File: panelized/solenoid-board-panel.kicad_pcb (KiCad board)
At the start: 2 copper layers, 99 x 94.5 mm, 216 parts, among them J1 JST_PH, J2 0.1" header, Q1 FDN339AN

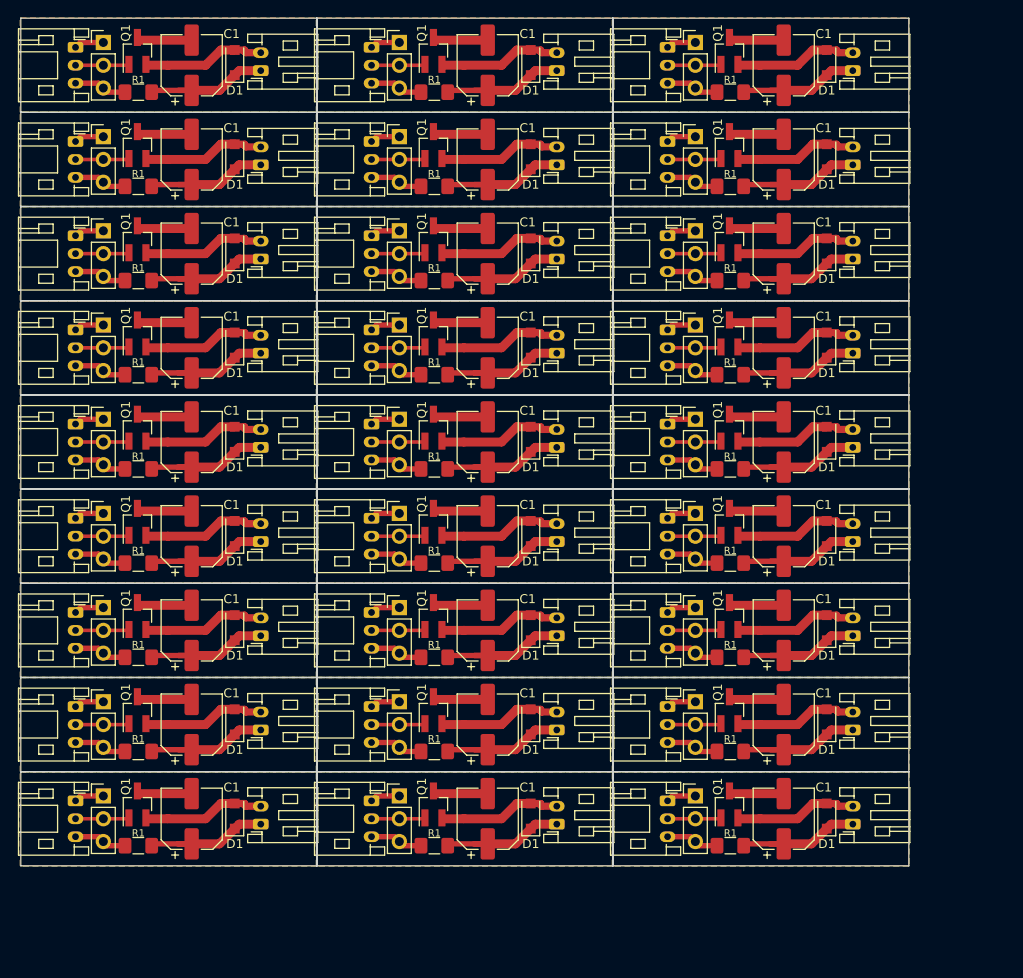
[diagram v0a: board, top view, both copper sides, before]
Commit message: updated panelized design
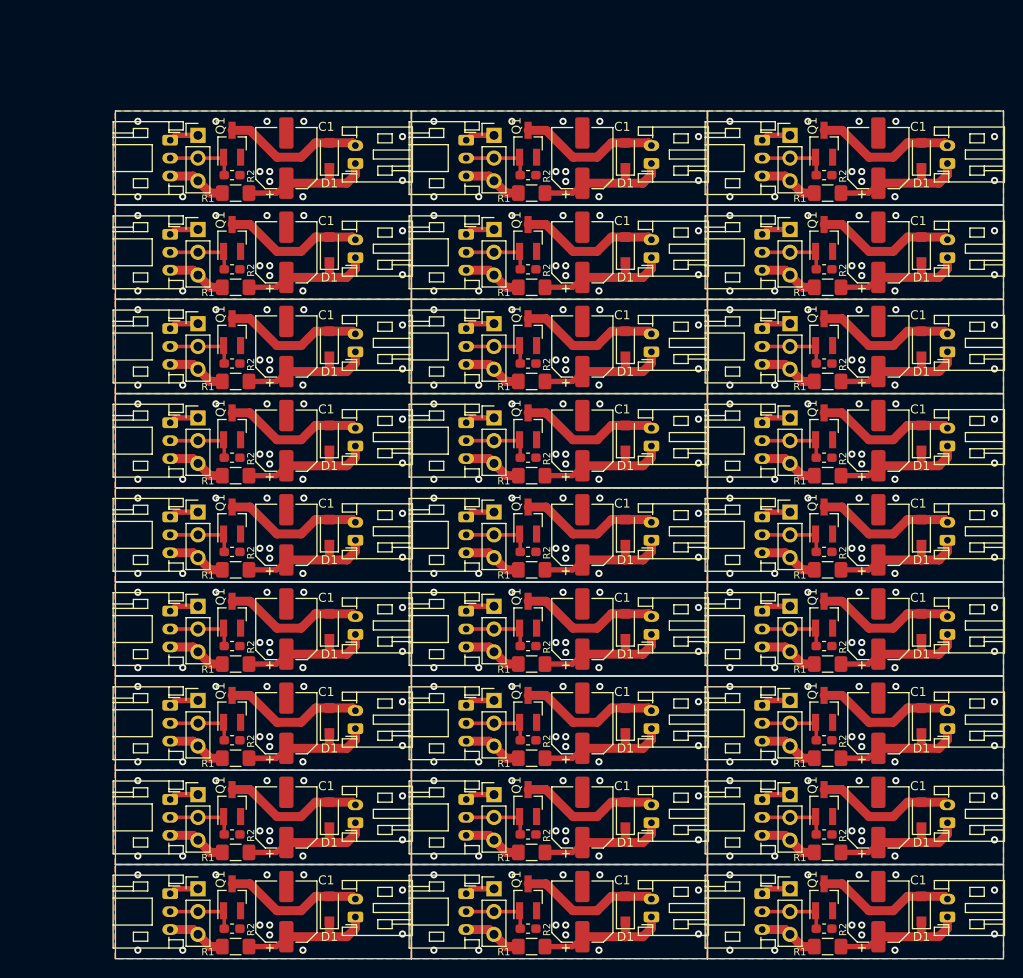
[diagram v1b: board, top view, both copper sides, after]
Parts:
- removed the C1 at (95.0, 99.2)
- removed the C1 at (95.0, 67.8)
- removed the C1 at (62.0, 67.8)
- removed the C1 at (29.1, 67.8)
- removed the C1 at (95.0, 57.2)
- removed the C1 at (62.0, 57.2)
- removed the C1 at (29.1, 57.2)
- removed the C1 at (95.0, 46.8)
- removed the C1 at (62.0, 46.8)
- removed the C1 at (29.1, 46.8)
- removed the C1 at (95.0, 36.2)
- removed the C1 at (62.0, 99.2)
- removed the C1 at (62.0, 36.2)
- removed the C1 at (29.1, 36.2)
- removed the C1 at (95.0, 25.8)
- removed the C1 at (62.0, 25.8)
- removed the C1 at (29.1, 25.8)
- removed the C1 at (95.0, 15.2)
- removed the C1 at (62.0, 15.2)
- removed the C1 at (29.1, 99.2)
- removed the C1 at (95.0, 88.8)
- removed the C1 at (62.0, 88.8)
- removed the C1 at (29.1, 88.8)
- removed the C1 at (95.0, 78.2)
- removed the C1 at (62.0, 78.2)
- removed the C1 at (29.1, 78.2)
- removed the D1 at (99.8, 99.0)
- removed the D1 at (99.8, 67.5)
- removed the D1 at (66.8, 67.5)
- removed the D1 at (33.9, 67.5)
- removed the D1 at (99.8, 57.0)
- removed the D1 at (66.8, 57.0)
- removed the D1 at (33.9, 57.0)
- removed the D1 at (99.8, 46.5)
- removed the D1 at (66.8, 46.5)
- removed the D1 at (33.9, 46.5)
- removed the D1 at (99.8, 36.0)
- removed the D1 at (66.8, 99.0)
- removed the D1 at (66.8, 36.0)
- removed the D1 at (33.9, 36.0)
- removed the D1 at (99.8, 25.4)
- removed the D1 at (66.8, 25.4)
- removed the D1 at (33.9, 25.4)
- removed the D1 at (99.8, 14.9)
- removed the D1 at (66.8, 14.9)
- removed the D1 at (33.9, 99.0)
- removed the D1 at (99.8, 88.5)
- removed the D1 at (66.8, 88.5)
- removed the D1 at (33.9, 88.5)
- removed the D1 at (99.8, 78.0)
- removed the D1 at (66.8, 78.0)
- removed the D1 at (33.9, 78.0)
- removed the G*** at (93.8, 99.8)
- removed the G*** at (93.8, 68.2)
- removed the G*** at (60.8, 68.2)
- removed the G*** at (27.8, 68.2)
- removed the G*** at (93.8, 57.8)
- removed the G*** at (60.8, 57.8)
- removed the G*** at (27.8, 57.8)
- removed the G*** at (93.8, 47.2)
- removed the G*** at (60.8, 47.2)
- removed the G*** at (27.8, 47.2)
- removed the G*** at (93.8, 36.8)
- removed the G*** at (60.8, 99.8)
- removed the G*** at (60.8, 36.8)
- removed the G*** at (27.8, 36.8)
- removed the G*** at (93.8, 26.2)
- removed the G*** at (60.8, 26.2)
- removed the G*** at (27.8, 26.2)
- removed the G*** at (93.8, 15.8)
- removed the G*** at (60.8, 15.8)
- removed the G*** at (27.8, 99.8)
- removed the G*** at (93.8, 89.2)
- removed the G*** at (60.8, 89.2)
- removed the G*** at (27.8, 89.2)
- removed the G*** at (93.8, 78.8)
- removed the G*** at (60.8, 78.8)
- removed the G*** at (27.8, 78.8)
- removed the J1 at (82.1, 97.2)
- removed the J1 at (82.1, 65.8)
- removed the J1 at (49.1, 65.8)
- removed the J1 at (16.1, 65.8)
- removed the J1 at (82.1, 55.2)
- removed the J1 at (49.1, 55.2)
- removed the J1 at (16.1, 55.2)
- removed the J1 at (82.1, 44.8)
- removed the J1 at (49.1, 44.8)
- removed the J1 at (16.1, 44.8)
- removed the J1 at (82.1, 34.2)
- removed the J1 at (49.1, 97.2)
- removed the J1 at (49.1, 34.2)
- removed the J1 at (16.1, 34.2)
- removed the J1 at (82.1, 23.8)
- removed the J1 at (49.1, 23.8)
- removed the J1 at (16.1, 23.8)
- removed the J1 at (82.1, 13.2)
- removed the J1 at (49.1, 13.2)
- removed the J1 at (16.1, 97.2)
- removed the J1 at (82.1, 86.8)
- removed the J1 at (49.1, 86.8)
- removed the J1 at (16.1, 86.8)
- removed the J1 at (82.1, 76.2)
- removed the J1 at (49.1, 76.2)
- removed the J1 at (16.1, 76.2)
- removed the J2 at (85.2, 96.7)
- removed the J2 at (85.2, 65.2)
- removed the J2 at (52.2, 65.2)
- removed the J2 at (19.2, 65.2)
- removed the J2 at (85.2, 54.7)
- removed the J2 at (52.2, 54.7)
- removed the J2 at (19.2, 54.7)
- removed the J2 at (85.2, 44.2)
- removed the J2 at (52.2, 44.2)
- removed the J2 at (19.2, 44.2)
- removed the J2 at (85.2, 33.7)
- removed the J2 at (52.2, 96.7)
- removed the J2 at (52.2, 33.7)
- removed the J2 at (19.2, 33.7)
- removed the J2 at (85.2, 23.2)
- removed the J2 at (52.2, 23.2)
- removed the J2 at (19.2, 23.2)
- removed the J2 at (85.2, 12.7)
- removed the J2 at (52.2, 12.7)
- removed the J2 at (19.2, 96.7)
- removed the J2 at (85.2, 86.2)
- removed the J2 at (52.2, 86.2)
- removed the J2 at (19.2, 86.2)
- removed the J2 at (85.2, 75.7)
- removed the J2 at (52.2, 75.7)
- removed the J2 at (19.2, 75.7)
- removed the L1 at (102.8, 99.8)
- removed the L1 at (102.8, 68.3)
- removed the L1 at (69.8, 68.3)
- removed the L1 at (36.8, 68.3)
- removed the L1 at (102.8, 57.9)
- removed the L1 at (69.8, 57.9)
- removed the L1 at (36.8, 57.9)
- removed the L1 at (102.8, 47.4)
- removed the L1 at (69.8, 47.4)
- removed the L1 at (36.8, 47.4)
- removed the L1 at (102.8, 36.9)
- removed the L1 at (69.8, 99.8)
- removed the L1 at (69.8, 36.9)
- removed the L1 at (36.8, 36.9)
- removed the L1 at (102.8, 26.4)
- removed the L1 at (69.8, 26.4)
- removed the L1 at (36.8, 26.4)
- removed the L1 at (102.8, 15.8)
- removed the L1 at (69.8, 15.8)
- removed the L1 at (36.8, 99.8)
- removed the L1 at (102.8, 89.3)
- removed the L1 at (69.8, 89.3)
- removed the L1 at (36.8, 89.3)
- removed the L1 at (102.8, 78.8)
- removed the L1 at (69.8, 78.8)
- removed the L1 at (36.8, 78.8)
- removed the Q1 at (89.0, 97.7)
- removed the Q1 at (89.0, 66.2)
- removed the Q1 at (56.0, 66.2)
- removed the Q1 at (23.0, 66.2)
- removed the Q1 at (89.0, 55.6)
- removed the Q1 at (56.0, 55.6)
- removed the Q1 at (23.0, 55.6)
- removed the Q1 at (89.0, 45.1)
- removed the Q1 at (56.0, 45.1)
- removed the Q1 at (23.0, 45.1)
- removed the Q1 at (89.0, 34.6)
- removed the Q1 at (56.0, 97.7)
- removed the Q1 at (56.0, 34.6)
- removed the Q1 at (23.0, 34.6)
- removed the Q1 at (89.0, 24.1)
- removed the Q1 at (56.0, 24.1)
- removed the Q1 at (23.0, 24.1)
- removed the Q1 at (89.0, 13.7)
- removed the Q1 at (56.0, 13.7)
- removed the Q1 at (23.0, 97.7)
- removed the Q1 at (89.0, 87.2)
- removed the Q1 at (56.0, 87.2)
- removed the Q1 at (23.0, 87.2)
- removed the Q1 at (89.0, 76.7)
- removed the Q1 at (56.0, 76.7)
- removed the Q1 at (23.0, 76.7)
- removed the R1 at (89.1, 102.2)
- removed the R1 at (89.1, 70.8)
- removed the R1 at (56.1, 70.8)
- removed the R1 at (23.1, 70.8)
- removed the R1 at (89.1, 60.2)
- removed the R1 at (56.1, 60.2)
- removed the R1 at (23.1, 60.2)
- removed the R1 at (89.1, 49.8)
- removed the R1 at (56.1, 49.8)
- removed the R1 at (23.1, 49.8)
- removed the R1 at (89.1, 39.2)
- removed the R1 at (56.1, 102.2)
- removed the R1 at (56.1, 39.2)
- removed the R1 at (23.1, 39.2)
- removed the R1 at (89.1, 28.8)
- removed the R1 at (56.1, 28.8)
- removed the R1 at (23.1, 28.8)
- removed the R1 at (89.1, 18.2)
- removed the R1 at (56.1, 18.2)
- removed the R1 at (23.1, 102.2)
- removed the R1 at (89.1, 91.8)
- removed the R1 at (56.1, 91.8)
- removed the R1 at (23.1, 91.8)
- removed the R1 at (89.1, 81.2)
- removed the R1 at (56.1, 81.2)
- removed the R1 at (23.1, 81.2)
- added C1: 220uF, Capacitor_SMD:CP_Elec_6.3x5.4, F.Cu at (105.6, 109.6)
- added C1: 220uF, Capacitor_SMD:CP_Elec_6.3x5.4, F.Cu at (105.6, 78.1)
- added C1: 220uF, Capacitor_SMD:CP_Elec_6.3x5.4, F.Cu at (72.6, 78.1)
- added C1: 220uF, Capacitor_SMD:CP_Elec_6.3x5.4, F.Cu at (39.6, 78.1)
- added C1: 220uF, Capacitor_SMD:CP_Elec_6.3x5.4, F.Cu at (105.6, 67.6)
- added C1: 220uF, Capacitor_SMD:CP_Elec_6.3x5.4, F.Cu at (72.6, 67.6)
- added C1: 220uF, Capacitor_SMD:CP_Elec_6.3x5.4, F.Cu at (39.6, 67.6)
- added C1: 220uF, Capacitor_SMD:CP_Elec_6.3x5.4, F.Cu at (105.6, 57.1)
- added C1: 220uF, Capacitor_SMD:CP_Elec_6.3x5.4, F.Cu at (72.6, 57.1)
- added C1: 220uF, Capacitor_SMD:CP_Elec_6.3x5.4, F.Cu at (39.6, 57.1)
- added C1: 220uF, Capacitor_SMD:CP_Elec_6.3x5.4, F.Cu at (105.6, 46.6)
- added C1: 220uF, Capacitor_SMD:CP_Elec_6.3x5.4, F.Cu at (72.6, 109.6)
- added C1: 220uF, Capacitor_SMD:CP_Elec_6.3x5.4, F.Cu at (72.6, 46.6)
- added C1: 220uF, Capacitor_SMD:CP_Elec_6.3x5.4, F.Cu at (39.6, 46.6)
- added C1: 220uF, Capacitor_SMD:CP_Elec_6.3x5.4, F.Cu at (105.6, 36.1)
- added C1: 220uF, Capacitor_SMD:CP_Elec_6.3x5.4, F.Cu at (72.6, 36.1)
- added C1: 220uF, Capacitor_SMD:CP_Elec_6.3x5.4, F.Cu at (39.6, 36.1)
- added C1: 220uF, Capacitor_SMD:CP_Elec_6.3x5.4, F.Cu at (105.6, 25.6)
- added C1: 220uF, Capacitor_SMD:CP_Elec_6.3x5.4, F.Cu at (72.6, 25.6)
- added C1: 220uF, Capacitor_SMD:CP_Elec_6.3x5.4, F.Cu at (39.6, 109.6)
- added C1: 220uF, Capacitor_SMD:CP_Elec_6.3x5.4, F.Cu at (105.6, 99.1)
- added C1: 220uF, Capacitor_SMD:CP_Elec_6.3x5.4, F.Cu at (72.6, 99.1)
- added C1: 220uF, Capacitor_SMD:CP_Elec_6.3x5.4, F.Cu at (39.6, 99.1)
- added C1: 220uF, Capacitor_SMD:CP_Elec_6.3x5.4, F.Cu at (105.6, 88.6)
- added C1: 220uF, Capacitor_SMD:CP_Elec_6.3x5.4, F.Cu at (72.6, 88.6)
- added C1: 220uF, Capacitor_SMD:CP_Elec_6.3x5.4, F.Cu at (39.6, 88.6)
- added D1: 1N4007L, Diode_SMD:D_SOD-123F, F.Cu at (110.4, 109.3)
- added D1: 1N4007L, Diode_SMD:D_SOD-123F, F.Cu at (110.4, 77.8)
- added D1: 1N4007L, Diode_SMD:D_SOD-123F, F.Cu at (77.4, 77.8)
- added D1: 1N4007L, Diode_SMD:D_SOD-123F, F.Cu at (44.4, 77.8)
- added D1: 1N4007L, Diode_SMD:D_SOD-123F, F.Cu at (110.4, 67.3)
- added D1: 1N4007L, Diode_SMD:D_SOD-123F, F.Cu at (77.4, 67.3)
- added D1: 1N4007L, Diode_SMD:D_SOD-123F, F.Cu at (44.4, 67.3)
- added D1: 1N4007L, Diode_SMD:D_SOD-123F, F.Cu at (110.4, 56.8)
- added D1: 1N4007L, Diode_SMD:D_SOD-123F, F.Cu at (77.4, 56.8)
- added D1: 1N4007L, Diode_SMD:D_SOD-123F, F.Cu at (44.4, 56.8)
- added D1: 1N4007L, Diode_SMD:D_SOD-123F, F.Cu at (110.4, 46.3)
- added D1: 1N4007L, Diode_SMD:D_SOD-123F, F.Cu at (77.4, 109.3)
- added D1: 1N4007L, Diode_SMD:D_SOD-123F, F.Cu at (77.4, 46.3)
- added D1: 1N4007L, Diode_SMD:D_SOD-123F, F.Cu at (44.4, 46.3)
- added D1: 1N4007L, Diode_SMD:D_SOD-123F, F.Cu at (110.4, 35.8)
- added D1: 1N4007L, Diode_SMD:D_SOD-123F, F.Cu at (77.4, 35.8)
- added D1: 1N4007L, Diode_SMD:D_SOD-123F, F.Cu at (44.4, 35.8)
- added D1: 1N4007L, Diode_SMD:D_SOD-123F, F.Cu at (110.4, 25.3)
- added D1: 1N4007L, Diode_SMD:D_SOD-123F, F.Cu at (77.4, 25.3)
- added D1: 1N4007L, Diode_SMD:D_SOD-123F, F.Cu at (44.4, 109.3)
- added D1: 1N4007L, Diode_SMD:D_SOD-123F, F.Cu at (110.4, 98.8)
- added D1: 1N4007L, Diode_SMD:D_SOD-123F, F.Cu at (77.4, 98.8)
- added D1: 1N4007L, Diode_SMD:D_SOD-123F, F.Cu at (44.4, 98.8)
- added D1: 1N4007L, Diode_SMD:D_SOD-123F, F.Cu at (110.4, 88.3)
- added D1: 1N4007L, Diode_SMD:D_SOD-123F, F.Cu at (77.4, 88.3)
- added D1: 1N4007L, Diode_SMD:D_SOD-123F, F.Cu at (44.4, 88.3)
- added G***: LOGO, graphics:kiwi10mm, B.Cu at (104.3, 110.1)
- added G***: LOGO, graphics:kiwi10mm, B.Cu at (104.3, 78.6)
- added G***: LOGO, graphics:kiwi10mm, B.Cu at (71.3, 78.6)
- added G***: LOGO, graphics:kiwi10mm, B.Cu at (38.3, 78.6)
- added G***: LOGO, graphics:kiwi10mm, B.Cu at (104.3, 68.1)
- added G***: LOGO, graphics:kiwi10mm, B.Cu at (71.3, 68.1)
- added G***: LOGO, graphics:kiwi10mm, B.Cu at (38.3, 68.1)
- added G***: LOGO, graphics:kiwi10mm, B.Cu at (104.3, 57.6)
- added G***: LOGO, graphics:kiwi10mm, B.Cu at (71.3, 57.6)
- added G***: LOGO, graphics:kiwi10mm, B.Cu at (38.3, 57.6)
- added G***: LOGO, graphics:kiwi10mm, B.Cu at (104.3, 47.1)
- added G***: LOGO, graphics:kiwi10mm, B.Cu at (71.3, 110.1)
- added G***: LOGO, graphics:kiwi10mm, B.Cu at (71.3, 47.1)
- added G***: LOGO, graphics:kiwi10mm, B.Cu at (38.3, 47.1)
- added G***: LOGO, graphics:kiwi10mm, B.Cu at (104.3, 36.6)
- added G***: LOGO, graphics:kiwi10mm, B.Cu at (71.3, 36.6)
- added G***: LOGO, graphics:kiwi10mm, B.Cu at (38.3, 36.6)
- added G***: LOGO, graphics:kiwi10mm, B.Cu at (104.3, 26.1)
- added G***: LOGO, graphics:kiwi10mm, B.Cu at (71.3, 26.1)
- added G***: LOGO, graphics:kiwi10mm, B.Cu at (38.3, 110.1)
- added G***: LOGO, graphics:kiwi10mm, B.Cu at (104.3, 99.6)
- added G***: LOGO, graphics:kiwi10mm, B.Cu at (71.3, 99.6)
- added G***: LOGO, graphics:kiwi10mm, B.Cu at (38.3, 99.6)
- added G***: LOGO, graphics:kiwi10mm, B.Cu at (104.3, 89.1)
- added G***: LOGO, graphics:kiwi10mm, B.Cu at (71.3, 89.1)
- added G***: LOGO, graphics:kiwi10mm, B.Cu at (38.3, 89.1)
- added J1: JST_PH, Connector_JST:JST_PH_S3B-PH-K_1x03_P2.00mm_Horizontal, F.Cu at (92.7, 107.6)
- added J1: JST_PH, Connector_JST:JST_PH_S3B-PH-K_1x03_P2.00mm_Horizontal, F.Cu at (92.7, 76.1)
- added J1: JST_PH, Connector_JST:JST_PH_S3B-PH-K_1x03_P2.00mm_Horizontal, F.Cu at (59.6, 76.1)
- added J1: JST_PH, Connector_JST:JST_PH_S3B-PH-K_1x03_P2.00mm_Horizontal, F.Cu at (26.6, 76.1)
- added J1: JST_PH, Connector_JST:JST_PH_S3B-PH-K_1x03_P2.00mm_Horizontal, F.Cu at (92.7, 65.6)
- added J1: JST_PH, Connector_JST:JST_PH_S3B-PH-K_1x03_P2.00mm_Horizontal, F.Cu at (59.6, 65.6)
- added J1: JST_PH, Connector_JST:JST_PH_S3B-PH-K_1x03_P2.00mm_Horizontal, F.Cu at (26.6, 65.6)
- added J1: JST_PH, Connector_JST:JST_PH_S3B-PH-K_1x03_P2.00mm_Horizontal, F.Cu at (92.7, 55.1)
- added J1: JST_PH, Connector_JST:JST_PH_S3B-PH-K_1x03_P2.00mm_Horizontal, F.Cu at (59.6, 55.1)
- added J1: JST_PH, Connector_JST:JST_PH_S3B-PH-K_1x03_P2.00mm_Horizontal, F.Cu at (26.6, 55.1)
- added J1: JST_PH, Connector_JST:JST_PH_S3B-PH-K_1x03_P2.00mm_Horizontal, F.Cu at (92.7, 44.6)
- added J1: JST_PH, Connector_JST:JST_PH_S3B-PH-K_1x03_P2.00mm_Horizontal, F.Cu at (59.6, 107.6)
- added J1: JST_PH, Connector_JST:JST_PH_S3B-PH-K_1x03_P2.00mm_Horizontal, F.Cu at (59.6, 44.6)
- added J1: JST_PH, Connector_JST:JST_PH_S3B-PH-K_1x03_P2.00mm_Horizontal, F.Cu at (26.6, 44.6)
- added J1: JST_PH, Connector_JST:JST_PH_S3B-PH-K_1x03_P2.00mm_Horizontal, F.Cu at (92.7, 34.1)
- added J1: JST_PH, Connector_JST:JST_PH_S3B-PH-K_1x03_P2.00mm_Horizontal, F.Cu at (59.6, 34.1)
- added J1: JST_PH, Connector_JST:JST_PH_S3B-PH-K_1x03_P2.00mm_Horizontal, F.Cu at (26.6, 34.1)
- added J1: JST_PH, Connector_JST:JST_PH_S3B-PH-K_1x03_P2.00mm_Horizontal, F.Cu at (92.7, 23.6)
- added J1: JST_PH, Connector_JST:JST_PH_S3B-PH-K_1x03_P2.00mm_Horizontal, F.Cu at (59.6, 23.6)
- added J1: JST_PH, Connector_JST:JST_PH_S3B-PH-K_1x03_P2.00mm_Horizontal, F.Cu at (26.6, 107.6)
- added J1: JST_PH, Connector_JST:JST_PH_S3B-PH-K_1x03_P2.00mm_Horizontal, F.Cu at (92.7, 97.1)
- added J1: JST_PH, Connector_JST:JST_PH_S3B-PH-K_1x03_P2.00mm_Horizontal, F.Cu at (59.6, 97.1)
- added J1: JST_PH, Connector_JST:JST_PH_S3B-PH-K_1x03_P2.00mm_Horizontal, F.Cu at (26.6, 97.1)
- added J1: JST_PH, Connector_JST:JST_PH_S3B-PH-K_1x03_P2.00mm_Horizontal, F.Cu at (92.7, 86.6)
- added J1: JST_PH, Connector_JST:JST_PH_S3B-PH-K_1x03_P2.00mm_Horizontal, F.Cu at (59.6, 86.6)
- added J1: JST_PH, Connector_JST:JST_PH_S3B-PH-K_1x03_P2.00mm_Horizontal, F.Cu at (26.6, 86.6)
- added J2: 0.1" header, Connector_PinHeader_2.54mm:PinHeader_1x03_P2.54mm_Vertical, F.Cu at (95.8, 107.1)
- added J2: 0.1" header, Connector_PinHeader_2.54mm:PinHeader_1x03_P2.54mm_Vertical, F.Cu at (95.8, 75.6)
- added J2: 0.1" header, Connector_PinHeader_2.54mm:PinHeader_1x03_P2.54mm_Vertical, F.Cu at (62.8, 75.6)
- added J2: 0.1" header, Connector_PinHeader_2.54mm:PinHeader_1x03_P2.54mm_Vertical, F.Cu at (29.8, 75.6)
- added J2: 0.1" header, Connector_PinHeader_2.54mm:PinHeader_1x03_P2.54mm_Vertical, F.Cu at (95.8, 65.1)
- added J2: 0.1" header, Connector_PinHeader_2.54mm:PinHeader_1x03_P2.54mm_Vertical, F.Cu at (62.8, 65.1)
- added J2: 0.1" header, Connector_PinHeader_2.54mm:PinHeader_1x03_P2.54mm_Vertical, F.Cu at (29.8, 65.1)
- added J2: 0.1" header, Connector_PinHeader_2.54mm:PinHeader_1x03_P2.54mm_Vertical, F.Cu at (95.8, 54.6)
- added J2: 0.1" header, Connector_PinHeader_2.54mm:PinHeader_1x03_P2.54mm_Vertical, F.Cu at (62.8, 54.6)
- added J2: 0.1" header, Connector_PinHeader_2.54mm:PinHeader_1x03_P2.54mm_Vertical, F.Cu at (29.8, 54.6)
- added J2: 0.1" header, Connector_PinHeader_2.54mm:PinHeader_1x03_P2.54mm_Vertical, F.Cu at (95.8, 44.1)
- added J2: 0.1" header, Connector_PinHeader_2.54mm:PinHeader_1x03_P2.54mm_Vertical, F.Cu at (62.8, 107.1)
- added J2: 0.1" header, Connector_PinHeader_2.54mm:PinHeader_1x03_P2.54mm_Vertical, F.Cu at (62.8, 44.1)
- added J2: 0.1" header, Connector_PinHeader_2.54mm:PinHeader_1x03_P2.54mm_Vertical, F.Cu at (29.8, 44.1)
- added J2: 0.1" header, Connector_PinHeader_2.54mm:PinHeader_1x03_P2.54mm_Vertical, F.Cu at (95.8, 33.6)
- added J2: 0.1" header, Connector_PinHeader_2.54mm:PinHeader_1x03_P2.54mm_Vertical, F.Cu at (62.8, 33.6)
- added J2: 0.1" header, Connector_PinHeader_2.54mm:PinHeader_1x03_P2.54mm_Vertical, F.Cu at (29.8, 33.6)
- added J2: 0.1" header, Connector_PinHeader_2.54mm:PinHeader_1x03_P2.54mm_Vertical, F.Cu at (95.8, 23.1)
- added J2: 0.1" header, Connector_PinHeader_2.54mm:PinHeader_1x03_P2.54mm_Vertical, F.Cu at (62.8, 23.1)
- added J2: 0.1" header, Connector_PinHeader_2.54mm:PinHeader_1x03_P2.54mm_Vertical, F.Cu at (29.8, 107.1)
- added J2: 0.1" header, Connector_PinHeader_2.54mm:PinHeader_1x03_P2.54mm_Vertical, F.Cu at (95.8, 96.6)
- added J2: 0.1" header, Connector_PinHeader_2.54mm:PinHeader_1x03_P2.54mm_Vertical, F.Cu at (62.8, 96.6)
- added J2: 0.1" header, Connector_PinHeader_2.54mm:PinHeader_1x03_P2.54mm_Vertical, F.Cu at (29.8, 96.6)
- added J2: 0.1" header, Connector_PinHeader_2.54mm:PinHeader_1x03_P2.54mm_Vertical, F.Cu at (95.8, 86.1)
- added J2: 0.1" header, Connector_PinHeader_2.54mm:PinHeader_1x03_P2.54mm_Vertical, F.Cu at (62.8, 86.1)
- added J2: 0.1" header, Connector_PinHeader_2.54mm:PinHeader_1x03_P2.54mm_Vertical, F.Cu at (29.8, 86.1)
- added L1: solenoid, Connector_JST:JST_PH_S2B-PH-K_1x02_P2.00mm_Horizontal, F.Cu at (113.3, 110.2)
- added L1: solenoid, Connector_JST:JST_PH_S2B-PH-K_1x02_P2.00mm_Horizontal, F.Cu at (113.3, 78.7)
- added L1: solenoid, Connector_JST:JST_PH_S2B-PH-K_1x02_P2.00mm_Horizontal, F.Cu at (80.3, 78.7)
- added L1: solenoid, Connector_JST:JST_PH_S2B-PH-K_1x02_P2.00mm_Horizontal, F.Cu at (47.3, 78.7)
- added L1: solenoid, Connector_JST:JST_PH_S2B-PH-K_1x02_P2.00mm_Horizontal, F.Cu at (113.3, 68.2)
- added L1: solenoid, Connector_JST:JST_PH_S2B-PH-K_1x02_P2.00mm_Horizontal, F.Cu at (80.3, 68.2)
- added L1: solenoid, Connector_JST:JST_PH_S2B-PH-K_1x02_P2.00mm_Horizontal, F.Cu at (47.3, 68.2)
- added L1: solenoid, Connector_JST:JST_PH_S2B-PH-K_1x02_P2.00mm_Horizontal, F.Cu at (113.3, 57.7)
- added L1: solenoid, Connector_JST:JST_PH_S2B-PH-K_1x02_P2.00mm_Horizontal, F.Cu at (80.3, 57.7)
- added L1: solenoid, Connector_JST:JST_PH_S2B-PH-K_1x02_P2.00mm_Horizontal, F.Cu at (47.3, 57.7)
- added L1: solenoid, Connector_JST:JST_PH_S2B-PH-K_1x02_P2.00mm_Horizontal, F.Cu at (113.3, 47.2)
- added L1: solenoid, Connector_JST:JST_PH_S2B-PH-K_1x02_P2.00mm_Horizontal, F.Cu at (80.3, 110.2)
- added L1: solenoid, Connector_JST:JST_PH_S2B-PH-K_1x02_P2.00mm_Horizontal, F.Cu at (80.3, 47.2)
- added L1: solenoid, Connector_JST:JST_PH_S2B-PH-K_1x02_P2.00mm_Horizontal, F.Cu at (47.3, 47.2)
- added L1: solenoid, Connector_JST:JST_PH_S2B-PH-K_1x02_P2.00mm_Horizontal, F.Cu at (113.3, 36.7)
- added L1: solenoid, Connector_JST:JST_PH_S2B-PH-K_1x02_P2.00mm_Horizontal, F.Cu at (80.3, 36.7)
- added L1: solenoid, Connector_JST:JST_PH_S2B-PH-K_1x02_P2.00mm_Horizontal, F.Cu at (47.3, 36.7)
- added L1: solenoid, Connector_JST:JST_PH_S2B-PH-K_1x02_P2.00mm_Horizontal, F.Cu at (113.3, 26.2)
- added L1: solenoid, Connector_JST:JST_PH_S2B-PH-K_1x02_P2.00mm_Horizontal, F.Cu at (80.3, 26.2)
- added L1: solenoid, Connector_JST:JST_PH_S2B-PH-K_1x02_P2.00mm_Horizontal, F.Cu at (47.3, 110.2)
- added L1: solenoid, Connector_JST:JST_PH_S2B-PH-K_1x02_P2.00mm_Horizontal, F.Cu at (113.3, 99.7)
- added L1: solenoid, Connector_JST:JST_PH_S2B-PH-K_1x02_P2.00mm_Horizontal, F.Cu at (80.3, 99.7)
- added L1: solenoid, Connector_JST:JST_PH_S2B-PH-K_1x02_P2.00mm_Horizontal, F.Cu at (47.3, 99.7)
- added L1: solenoid, Connector_JST:JST_PH_S2B-PH-K_1x02_P2.00mm_Horizontal, F.Cu at (113.3, 89.2)
- added L1: solenoid, Connector_JST:JST_PH_S2B-PH-K_1x02_P2.00mm_Horizontal, F.Cu at (80.3, 89.2)
- added L1: solenoid, Connector_JST:JST_PH_S2B-PH-K_1x02_P2.00mm_Horizontal, F.Cu at (47.3, 89.2)
- added Q1: FDN339AN, Package_TO_SOT_SMD:SOT-23_Handsoldering, F.Cu at (99.5, 108.0)
- added Q1: FDN339AN, Package_TO_SOT_SMD:SOT-23_Handsoldering, F.Cu at (99.5, 76.5)
- added Q1: FDN339AN, Package_TO_SOT_SMD:SOT-23_Handsoldering, F.Cu at (66.5, 76.5)
- added Q1: FDN339AN, Package_TO_SOT_SMD:SOT-23_Handsoldering, F.Cu at (33.5, 76.5)
- added Q1: FDN339AN, Package_TO_SOT_SMD:SOT-23_Handsoldering, F.Cu at (99.5, 66.0)
- added Q1: FDN339AN, Package_TO_SOT_SMD:SOT-23_Handsoldering, F.Cu at (66.5, 66.0)
- added Q1: FDN339AN, Package_TO_SOT_SMD:SOT-23_Handsoldering, F.Cu at (33.5, 66.0)
- added Q1: FDN339AN, Package_TO_SOT_SMD:SOT-23_Handsoldering, F.Cu at (99.5, 55.5)
- added Q1: FDN339AN, Package_TO_SOT_SMD:SOT-23_Handsoldering, F.Cu at (66.5, 55.5)
- added Q1: FDN339AN, Package_TO_SOT_SMD:SOT-23_Handsoldering, F.Cu at (33.5, 55.5)
- added Q1: FDN339AN, Package_TO_SOT_SMD:SOT-23_Handsoldering, F.Cu at (99.5, 45.0)
- added Q1: FDN339AN, Package_TO_SOT_SMD:SOT-23_Handsoldering, F.Cu at (66.5, 108.0)
- added Q1: FDN339AN, Package_TO_SOT_SMD:SOT-23_Handsoldering, F.Cu at (66.5, 45.0)
- added Q1: FDN339AN, Package_TO_SOT_SMD:SOT-23_Handsoldering, F.Cu at (33.5, 45.0)
- added Q1: FDN339AN, Package_TO_SOT_SMD:SOT-23_Handsoldering, F.Cu at (99.5, 34.5)
- added Q1: FDN339AN, Package_TO_SOT_SMD:SOT-23_Handsoldering, F.Cu at (66.5, 34.5)
- added Q1: FDN339AN, Package_TO_SOT_SMD:SOT-23_Handsoldering, F.Cu at (33.5, 34.5)
- added Q1: FDN339AN, Package_TO_SOT_SMD:SOT-23_Handsoldering, F.Cu at (99.5, 24.0)
- added Q1: FDN339AN, Package_TO_SOT_SMD:SOT-23_Handsoldering, F.Cu at (66.5, 24.0)
- added Q1: FDN339AN, Package_TO_SOT_SMD:SOT-23_Handsoldering, F.Cu at (33.5, 108.0)
- added Q1: FDN339AN, Package_TO_SOT_SMD:SOT-23_Handsoldering, F.Cu at (99.5, 97.5)
- added Q1: FDN339AN, Package_TO_SOT_SMD:SOT-23_Handsoldering, F.Cu at (66.5, 97.5)
- added Q1: FDN339AN, Package_TO_SOT_SMD:SOT-23_Handsoldering, F.Cu at (33.5, 97.5)
- added Q1: FDN339AN, Package_TO_SOT_SMD:SOT-23_Handsoldering, F.Cu at (99.5, 87.0)
- added Q1: FDN339AN, Package_TO_SOT_SMD:SOT-23_Handsoldering, F.Cu at (66.5, 87.0)
- added Q1: FDN339AN, Package_TO_SOT_SMD:SOT-23_Handsoldering, F.Cu at (33.5, 87.0)
- added R1: 22R, Resistor_SMD:R_1206_3216Metric_Pad1.42x1.75mm_HandSolder, F.Cu at (100.0, 113.5)
- added R1: 22R, Resistor_SMD:R_1206_3216Metric_Pad1.42x1.75mm_HandSolder, F.Cu at (100.0, 82.0)
- added R1: 22R, Resistor_SMD:R_1206_3216Metric_Pad1.42x1.75mm_HandSolder, F.Cu at (67.0, 82.0)
- added R1: 22R, Resistor_SMD:R_1206_3216Metric_Pad1.42x1.75mm_HandSolder, F.Cu at (34.0, 82.0)
- added R1: 22R, Resistor_SMD:R_1206_3216Metric_Pad1.42x1.75mm_HandSolder, F.Cu at (100.0, 71.5)
- added R1: 22R, Resistor_SMD:R_1206_3216Metric_Pad1.42x1.75mm_HandSolder, F.Cu at (67.0, 71.5)
- added R1: 22R, Resistor_SMD:R_1206_3216Metric_Pad1.42x1.75mm_HandSolder, F.Cu at (34.0, 71.5)
- added R1: 22R, Resistor_SMD:R_1206_3216Metric_Pad1.42x1.75mm_HandSolder, F.Cu at (100.0, 61.0)
- added R1: 22R, Resistor_SMD:R_1206_3216Metric_Pad1.42x1.75mm_HandSolder, F.Cu at (67.0, 61.0)
- added R1: 22R, Resistor_SMD:R_1206_3216Metric_Pad1.42x1.75mm_HandSolder, F.Cu at (34.0, 61.0)
- added R1: 22R, Resistor_SMD:R_1206_3216Metric_Pad1.42x1.75mm_HandSolder, F.Cu at (100.0, 50.5)
- added R1: 22R, Resistor_SMD:R_1206_3216Metric_Pad1.42x1.75mm_HandSolder, F.Cu at (67.0, 113.5)
- added R1: 22R, Resistor_SMD:R_1206_3216Metric_Pad1.42x1.75mm_HandSolder, F.Cu at (67.0, 50.5)
- added R1: 22R, Resistor_SMD:R_1206_3216Metric_Pad1.42x1.75mm_HandSolder, F.Cu at (34.0, 50.5)
- added R1: 22R, Resistor_SMD:R_1206_3216Metric_Pad1.42x1.75mm_HandSolder, F.Cu at (100.0, 40.0)
- added R1: 22R, Resistor_SMD:R_1206_3216Metric_Pad1.42x1.75mm_HandSolder, F.Cu at (67.0, 40.0)
- added R1: 22R, Resistor_SMD:R_1206_3216Metric_Pad1.42x1.75mm_HandSolder, F.Cu at (34.0, 40.0)
- added R1: 22R, Resistor_SMD:R_1206_3216Metric_Pad1.42x1.75mm_HandSolder, F.Cu at (100.0, 29.5)
- added R1: 22R, Resistor_SMD:R_1206_3216Metric_Pad1.42x1.75mm_HandSolder, F.Cu at (67.0, 29.5)
- added R1: 22R, Resistor_SMD:R_1206_3216Metric_Pad1.42x1.75mm_HandSolder, F.Cu at (34.0, 113.5)
- added R1: 22R, Resistor_SMD:R_1206_3216Metric_Pad1.42x1.75mm_HandSolder, F.Cu at (100.0, 103.0)
- added R1: 22R, Resistor_SMD:R_1206_3216Metric_Pad1.42x1.75mm_HandSolder, F.Cu at (67.0, 103.0)
- added R1: 22R, Resistor_SMD:R_1206_3216Metric_Pad1.42x1.75mm_HandSolder, F.Cu at (34.0, 103.0)
- added R1: 22R, Resistor_SMD:R_1206_3216Metric_Pad1.42x1.75mm_HandSolder, F.Cu at (100.0, 92.5)
- added R1: 22R, Resistor_SMD:R_1206_3216Metric_Pad1.42x1.75mm_HandSolder, F.Cu at (67.0, 92.5)
- added R1: 22R, Resistor_SMD:R_1206_3216Metric_Pad1.42x1.75mm_HandSolder, F.Cu at (34.0, 92.5)
- added R2: 10k, Resistor_SMD:R_0603_1608Metric_Pad1.05x0.95mm_HandSolder, F.Cu at (99.5, 111.5)
- added R2: 10k, Resistor_SMD:R_0603_1608Metric_Pad1.05x0.95mm_HandSolder, F.Cu at (99.5, 80.0)
- added R2: 10k, Resistor_SMD:R_0603_1608Metric_Pad1.05x0.95mm_HandSolder, F.Cu at (66.5, 80.0)
- added R2: 10k, Resistor_SMD:R_0603_1608Metric_Pad1.05x0.95mm_HandSolder, F.Cu at (33.5, 80.0)
- added R2: 10k, Resistor_SMD:R_0603_1608Metric_Pad1.05x0.95mm_HandSolder, F.Cu at (99.5, 69.5)
- added R2: 10k, Resistor_SMD:R_0603_1608Metric_Pad1.05x0.95mm_HandSolder, F.Cu at (66.5, 69.5)
- added R2: 10k, Resistor_SMD:R_0603_1608Metric_Pad1.05x0.95mm_HandSolder, F.Cu at (33.5, 69.5)
- added R2: 10k, Resistor_SMD:R_0603_1608Metric_Pad1.05x0.95mm_HandSolder, F.Cu at (99.5, 59.0)
- added R2: 10k, Resistor_SMD:R_0603_1608Metric_Pad1.05x0.95mm_HandSolder, F.Cu at (66.5, 59.0)
- added R2: 10k, Resistor_SMD:R_0603_1608Metric_Pad1.05x0.95mm_HandSolder, F.Cu at (33.5, 59.0)
- added R2: 10k, Resistor_SMD:R_0603_1608Metric_Pad1.05x0.95mm_HandSolder, F.Cu at (99.5, 48.5)
- added R2: 10k, Resistor_SMD:R_0603_1608Metric_Pad1.05x0.95mm_HandSolder, F.Cu at (66.5, 111.5)
- added R2: 10k, Resistor_SMD:R_0603_1608Metric_Pad1.05x0.95mm_HandSolder, F.Cu at (66.5, 48.5)
- added R2: 10k, Resistor_SMD:R_0603_1608Metric_Pad1.05x0.95mm_HandSolder, F.Cu at (33.5, 48.5)
- added R2: 10k, Resistor_SMD:R_0603_1608Metric_Pad1.05x0.95mm_HandSolder, F.Cu at (99.5, 38.0)
- added R2: 10k, Resistor_SMD:R_0603_1608Metric_Pad1.05x0.95mm_HandSolder, F.Cu at (66.5, 38.0)
- added R2: 10k, Resistor_SMD:R_0603_1608Metric_Pad1.05x0.95mm_HandSolder, F.Cu at (33.5, 38.0)
- added R2: 10k, Resistor_SMD:R_0603_1608Metric_Pad1.05x0.95mm_HandSolder, F.Cu at (99.5, 27.5)
- added R2: 10k, Resistor_SMD:R_0603_1608Metric_Pad1.05x0.95mm_HandSolder, F.Cu at (66.5, 27.5)
- added R2: 10k, Resistor_SMD:R_0603_1608Metric_Pad1.05x0.95mm_HandSolder, F.Cu at (33.5, 27.5)
- added R2: 10k, Resistor_SMD:R_0603_1608Metric_Pad1.05x0.95mm_HandSolder, F.Cu at (33.5, 111.5)
- added R2: 10k, Resistor_SMD:R_0603_1608Metric_Pad1.05x0.95mm_HandSolder, F.Cu at (99.5, 101.0)
- added R2: 10k, Resistor_SMD:R_0603_1608Metric_Pad1.05x0.95mm_HandSolder, F.Cu at (66.5, 101.0)
- added R2: 10k, Resistor_SMD:R_0603_1608Metric_Pad1.05x0.95mm_HandSolder, F.Cu at (33.5, 101.0)
- added R2: 10k, Resistor_SMD:R_0603_1608Metric_Pad1.05x0.95mm_HandSolder, F.Cu at (99.5, 90.5)
- added R2: 10k, Resistor_SMD:R_0603_1608Metric_Pad1.05x0.95mm_HandSolder, F.Cu at (66.5, 90.5)
- added R2: 10k, Resistor_SMD:R_0603_1608Metric_Pad1.05x0.95mm_HandSolder, F.Cu at (33.5, 90.5)
- moved R1 15.6 mm to (34.0, 29.5)
- moved C1 14.8 mm to (39.6, 25.6)
- moved D1 14.8 mm to (44.4, 25.3)
- moved G*** 14.8 mm to (38.3, 26.1)
- moved J1 14.8 mm to (26.6, 23.6)
- moved J2 14.8 mm to (29.8, 23.1)
- moved L1 14.8 mm to (47.3, 26.2)
- moved Q1 14.8 mm to (33.5, 24.0)
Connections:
- Q1 pad 2: Net-(D1-Pad2) -> GND
- Q1 pad 3: GND -> Net-(D1-Pad2)
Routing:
- net GND: track 261.8 -> 89.7 mm, vias 0 -> 324
- net Net-(D1-Pad2): track 366.7 -> 426.1 mm
- net /FIRE!: track 161.8 -> 216.6 mm
- net Net-(C1-Pad1): track 395.7 -> 423.4 mm
- net +5V: track 160.0 -> 178.2 mm
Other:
- board text added: "v1.0.1"
